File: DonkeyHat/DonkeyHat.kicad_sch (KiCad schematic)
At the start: 11 parts, among them J1 GPIO, J2 Conn_01x02_Pin, U1 ProMicro

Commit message: Added 4-bit encoders
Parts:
- removed Encoder: Conn_01x03_Pin, Connector_PinHeader_2.54mm:PinHeader_1x03_P2.54mm_Vertical, symbol Connector:Conn_01x03_Pin
- added J2: Encoder 2, Connector_PinHeader_2.54mm:PinHeader_1x04_P2.54mm_Vertical, symbol Connector:Conn_01x04_Pin
- added J3: Encoder 1, Connector_PinHeader_2.54mm:PinHeader_1x04_P2.54mm_Vertical, symbol Connector:Conn_01x04_Pin
- renumbered J2 to 5V1
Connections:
- net +3V3: now also J2.2 (Pin_2), J3.2 (Pin_2)
- net +5V: now also U1.22 (RST), U1.24 (RAW)
- net +BATT: no longer U1.24 (RAW)
- net GND: now also J2.1 (Pin_1), J3.1 (Pin_1)
- net GPIO13/PWM1: now also J2.3 (Pin_3)
- net GPIO16: now also J3.3 (Pin_3)
- net GPIO5: now also J3.4 (Pin_4)
- net GPIO6: now also J2.4 (Pin_4)

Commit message: Switched encoders to RP2040
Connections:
- net GPIO13/PWM1: no longer J2.3 (Pin_3)
- net GPIO16: no longer J3.3 (Pin_3)
- net GPIO5: no longer J3.4 (Pin_4)
- net GPIO6: no longer J1.31 (Pin_31), J2.4 (Pin_4)
- net at U1.10 (E6): now also J2.4 (Pin_4)
- net at U1.14 (B2): now also J3.3 (Pin_3)
- net at U1.15 (B3): now also J3.4 (Pin_4)
- net at U1.9 (D7): now also J2.3 (Pin_3)
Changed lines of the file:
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@@
-	)
-	(junction
-		(at 34.29 68.58)
-		(diameter 0)
-		(color 0 0 0 0)
 	)
 	(junction
@@
 	(wire
 		(pts
-			(xy 43.18 92.71) (xy 43.18 97.79)
-		)
-		(stroke
-			(width 0)
-			(type solid)
-		)
-	)
-	(wire
-		(pts
 			(xy 76.2 33.02) (xy 76.2 43.18)
 		)
@@
 	(wire
 		(pts
-			(xy 27.94 97.79) (xy 43.18 97.79)
-		)
-		(stroke
-			(width 0)
-			(type solid)
+			(xy 113.03 90.17) (xy 113.03 111.76)
+		)
+		(stroke
+			(width 0)
+			(type default)
 		)
 	)
@@
 	(wire
 		(pts
+			(xy 25.4 90.17) (xy 27.94 90.17)
+		)
+		(stroke
+			(width 0)
+			(type default)
+		)
+	)
+	(wire
+		(pts
 			(xy 80.01 71.12) (xy 100.33 71.12)
 		)
@@
 	(wire
 		(pts
-			(xy 15.24 66.04) (xy 60.96 66.04)
-		)
-		(stroke
-			(width 0)
-			(type solid)
-		)
-	)
-	(wire
-		(pts
 			(xy 154.94 46.99) (xy 162.56 46.99)
 		)
@@
 	(wire
 		(pts
-			(xy 25.4 90.17) (xy 34.29 90.17)
-		)
-		(stroke
-			(width 0)
-			(type solid)
-		)
-	)
-	(wire
-		(pts
 			(xy 161.29 69.85) (xy 162.56 69.85)
 		)
@@
 	(wire
 		(pts
-			(xy 25.4 92.71) (xy 25.4 97.79)
-		)
-		(stroke
-			(width 0)
-			(type solid)
-		)
-	)
-	(wire
-		(pts
 			(xy 76.2 50.8) (xy 76.2 63.5)
 		)
@@
 	(wire
 		(pts
+			(xy 115.57 109.22) (xy 115.57 92.71)
+		)
+		(stroke
+			(width 0)
+			(type default)
+		)
+	)
+	(wire
+		(pts
 			(xy 152.4 49.53) (xy 162.56 49.53)
 		)
@@
 	(wire
 		(pts
-			(xy 27.94 63.5) (xy 27.94 97.79)
-		)
-		(stroke
-			(width 0)
-			(type solid)
+			(xy 43.18 92.71) (xy 49.53 92.71)
+		)
+		(stroke
+			(width 0)
+			(type default)
 		)
 	)
@@
 	(wire
 		(pts
-			(xy 43.18 90.17) (xy 80.01 90.17)
-		)
-		(stroke
-			(width 0)
-			(type default)
-		)
-	)
-	(wire
-		(pts
 			(xy 133.35 52.07) (xy 137.16 52.07)
 		)
@@
 	(wire
 		(pts
-			(xy 15.24 66.04) (xy 15.24 97.79)
-		)
-		(stroke
-			(width 0)
-			(type solid)
+			(xy 49.53 121.92) (xy 163.83 121.92)
+		)
+		(stroke
+			(width 0)
+			(type default)
 		)
 	)
@@
 	(wire
 		(pts
-			(xy 15.24 97.79) (xy 25.4 97.79)
-		)
-		(stroke
-			(width 0)
-			(type solid)
-		)
-	)
-	(wire
-		(pts
 			(xy 152.4 36.83) (xy 162.56 36.83)
 		)
@@
 	(wire
 		(pts
+			(xy 163.83 92.71) (xy 157.48 92.71)
+		)
+		(stroke
+			(width 0)
+			(type default)
+		)
+	)
+	(wire
+		(pts
 			(xy 31.75 55.88) (xy 60.96 55.88)
 		)
@@
 	(wire
 		(pts
+			(xy 121.92 90.17) (xy 113.03 90.17)
+		)
+		(stroke
+			(width 0)
+			(type default)
+		)
+	)
+	(wire
+		(pts
 			(xy 55.88 48.26) (xy 60.96 48.26)
 		)
@@
 	(wire
 		(pts
+			(xy 162.56 95.25) (xy 162.56 116.84)
+		)
+		(stroke
+			(width 0)
+			(type default)
+		)
+	)
+	(wire
+		(pts
 			(xy 124.46 41.91) (xy 134.62 41.91)
 		)
@@
 	(wire
 		(pts
+			(xy 46.99 90.17) (xy 43.18 90.17)
+		)
+		(stroke
+			(width 0)
+			(type default)
+		)
+	)
+	(wire
+		(pts
 			(xy 157.48 74.93) (xy 161.29 74.93)
 		)
@@
 	(wire
 		(pts
+			(xy 113.03 111.76) (xy 27.94 111.76)
+		)
+		(stroke
+			(width 0)
+			(type default)
+		)
+	)
+	(wire
+		(pts
 			(xy 73.66 40.64) (xy 100.33 40.64)
 		)
@@
 	(wire
 		(pts
+			(xy 49.53 92.71) (xy 49.53 121.92)
+		)
+		(stroke
+			(width 0)
+			(type default)
+		)
+	)
+	(wire
+		(pts
 			(xy 69.85 93.98) (xy 72.39 93.98)
 		)
@@
 	(wire
 		(pts
+			(xy 25.4 92.71) (xy 25.4 109.22)
+		)
+		(stroke
+			(width 0)
+			(type default)
+		)
+	)
+	(wire
+		(pts
 			(xy 166.37 106.68) (xy 166.37 72.39)
 		)
@@
 	(wire
 		(pts
+			(xy 115.57 92.71) (xy 121.92 92.71)
+		)
+		(stroke
+			(width 0)
+			(type default)
+		)
+	)
+	(wire
+		(pts
 			(xy 132.08 26.67) (xy 119.38 26.67)
 		)
@@
 	(wire
 		(pts
+			(xy 46.99 116.84) (xy 46.99 90.17)
+		)
+		(stroke
+			(width 0)
+			(type default)
+		)
+	)
+	(wire
+		(pts
 			(xy 41.91 15.24) (xy 49.53 15.24)
 		)
@@
 	(wire
 		(pts
+			(xy 157.48 95.25) (xy 162.56 95.25)
+		)
+		(stroke
+			(width 0)
+			(type default)
+		)
+	)
+	(wire
+		(pts
 			(xy 50.8 87.63) (xy 72.39 87.63)
 		)
@@
 	(wire
 		(pts
-			(xy 34.29 68.58) (xy 34.29 90.17)
-		)
-		(stroke
-			(width 0)
-			(type solid)
-		)
-	)
-	(wire
-		(pts
 			(xy 26.67 30.48) (xy 60.96 30.48)
 		)
@@
 	(wire
 		(pts
+			(xy 163.83 121.92) (xy 163.83 92.71)
+		)
+		(stroke
+			(width 0)
+			(type default)
+		)
+	)
+	(wire
+		(pts
 			(xy 137.16 34.29) (xy 132.08 34.29)
 		)
@@
 	(wire
 		(pts
+			(xy 162.56 116.84) (xy 46.99 116.84)
+		)
+		(stroke
+			(width 0)
+			(type default)
+		)
+	)
+	(wire
+		(pts
 			(xy 73.66 53.34) (xy 100.33 53.34)
 		)
@@
 	(wire
 		(pts
-			(xy 60.96 68.58) (xy 34.29 68.58)
-		)
-		(stroke
-			(width 0)
-			(type solid)
-		)
-	)
-	(wire
-		(pts
 			(xy 147.32 57.15) (xy 152.4 57.15)
 		)
@@
 	(wire
 		(pts
-			(xy 34.29 68.58) (xy 31.75 68.58)
+			(xy 25.4 109.22) (xy 115.57 109.22)
+		)
+		(stroke
+			(width 0)
+			(type default)
+		)
+	)
+	(wire
+		(pts
+			(xy 31.75 68.58) (xy 60.96 68.58)
 		)
 		(stroke
@@
 		)
 		(stroke
+			(width 0)
+			(type default)
+		)
+	)
+	(wire
+		(pts
+			(xy 27.94 111.76) (xy 27.94 90.17)
+		)
+		(stroke

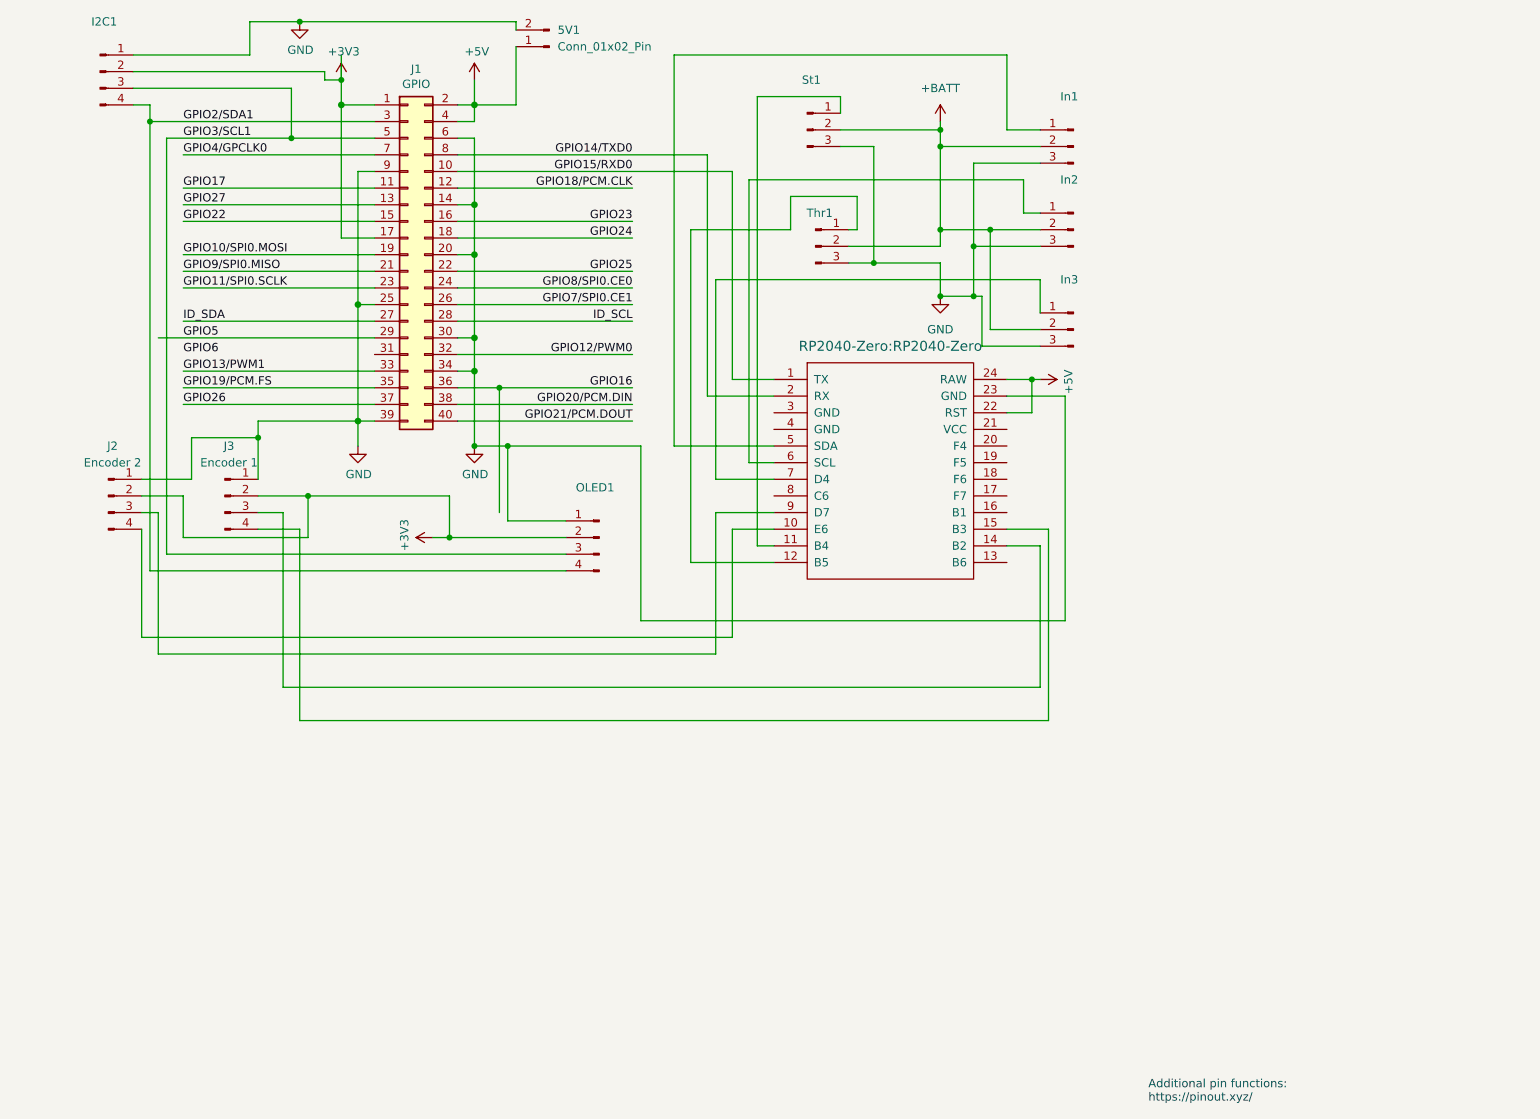
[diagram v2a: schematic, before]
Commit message: catellated pins
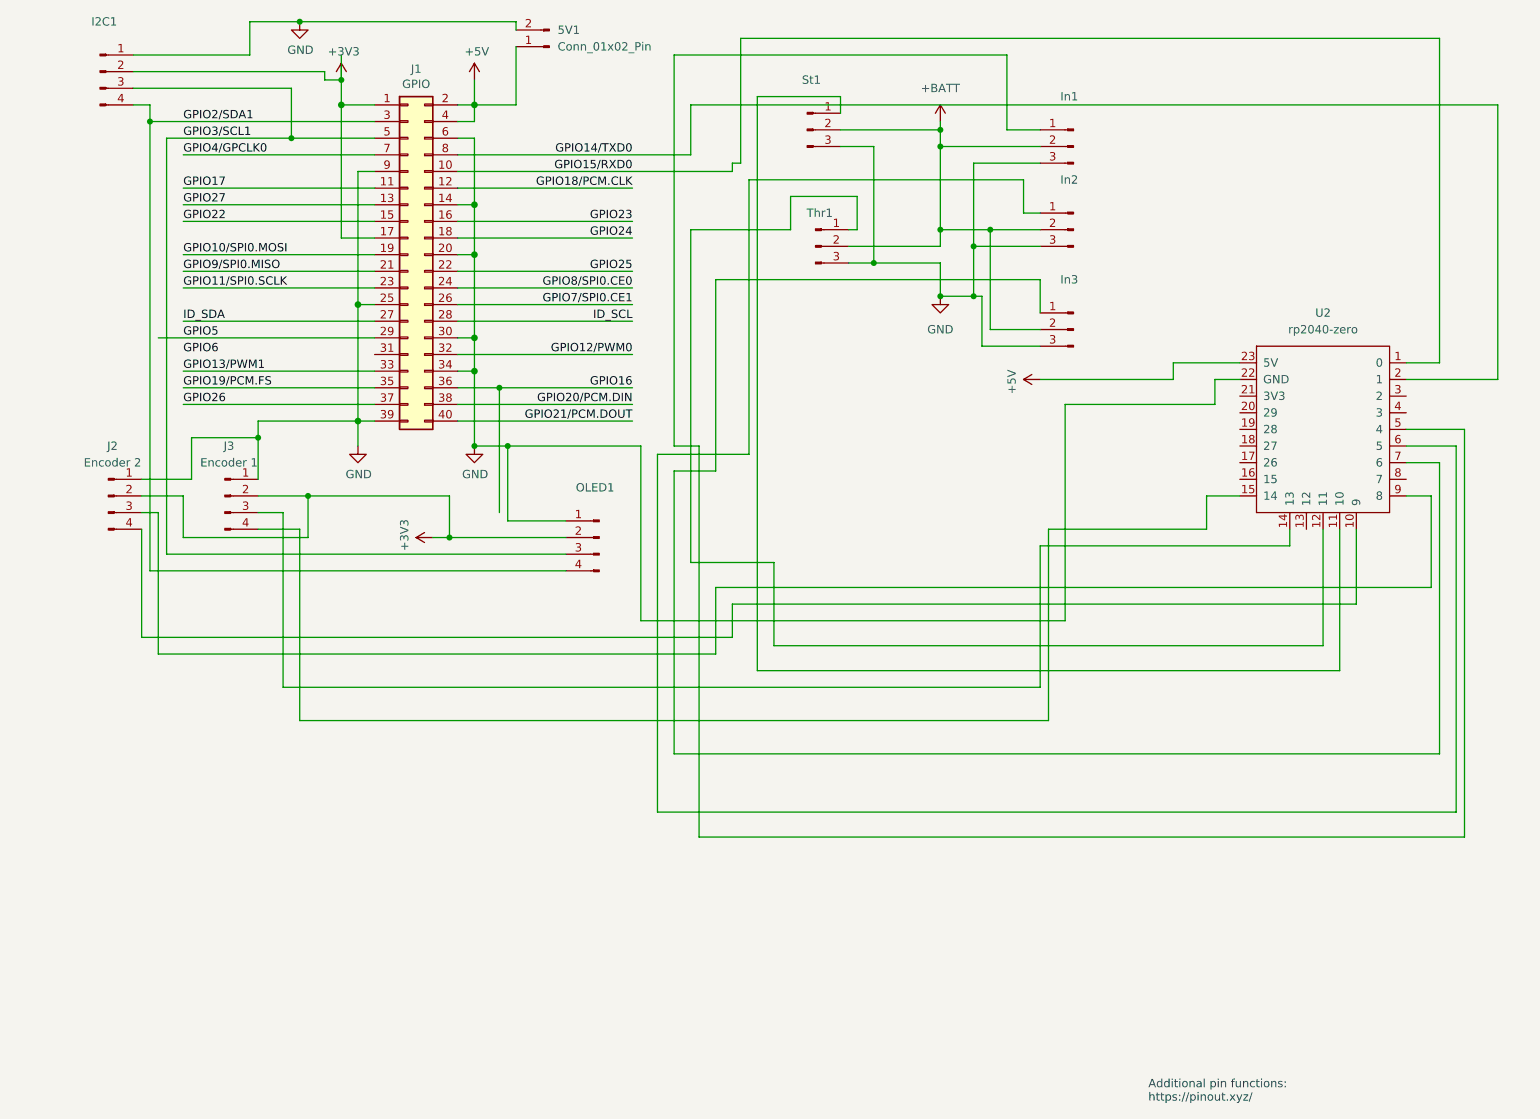
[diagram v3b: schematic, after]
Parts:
- removed U1: ProMicro, RP2040-Zero:RP2040-Zero, symbol promicro:ProMicro
- added U2: rp2040-zero, symbol mcu:rp2040-zero
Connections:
- net +5V: now also U2.23 (5V)
- net GND: now also U2.22 (GND)
- net GPIO14/TXD0: now also U2.2 (1)
- net GPIO15/RXD0: now also U2.1 (0)
- net at Thr1.1 (Pin_1): now also U2.12 (11)
- net at J2.3 (Pin_3): now also U2.9 (8)
- net at J2.4 (Pin_4): now also U2.10 (9)
- net at St1.1 (Pin_1): now also U2.11 (10)
- net at J3.3 (Pin_3): now also U2.14 (13)
- net at J3.4 (Pin_4): now also U2.15 (14)
- net at In1.1 (Pin_1): now also U2.5 (4)
- net at In2.1 (Pin_1): now also U2.6 (5)
- net at In3.1 (Pin_1): now also U2.7 (6)

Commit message: routed
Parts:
- U2: footprint (none) -> mcu:rp2040-zero-tht
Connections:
- net at J2.3 (Pin_3): now also U2.16 (15); no longer U2.9 (8)
- net at J3.3 (Pin_3): now also U2.19 (28); no longer U2.14 (13)
- net at U2.17 (26): now also In2.1 (Pin_1)
- net at U2.18 (27): now also In3.1 (Pin_1)
- net at U2.20 (29): now also In1.1 (Pin_1)
- net at U2.5 (4): no longer In1.1 (Pin_1)
- net at U2.6 (5): no longer In2.1 (Pin_1)
- net at U2.7 (6): no longer In3.1 (Pin_1)
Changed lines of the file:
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@@
-	(wire
-		(pts
-			(xy 226.06 135.89) (xy 226.06 80.01)
-		)
-		(stroke
-			(width 0)
-			(type default)
-		)
-	)
 	(wire
 		(pts
@@
 	(wire
 		(pts
+			(xy 193.04 80.01) (xy 186.69 80.01)
+		)
+		(stroke
+			(width 0)
+			(type default)
+		)
+	)
+	(wire
+		(pts
 			(xy 162.56 54.61) (xy 162.56 59.69)
 		)
@@
 	(wire
 		(pts
-			(xy 222.25 101.6) (xy 222.25 87.63)
-		)
-		(stroke
-			(width 0)
-			(type default)
-		)
-	)
-	(wire
-		(pts
 			(xy 208.28 92.71) (xy 208.28 114.3)
 		)
@@
 	(wire
 		(pts
+			(xy 162.56 77.47) (xy 193.04 77.47)
+		)
+		(stroke
+			(width 0)
+			(type default)
+		)
+	)
+	(wire
+		(pts
 			(xy 58.42 38.1) (xy 60.96 38.1)
 		)
@@
 	(wire
 		(pts
+			(xy 193.04 85.09) (xy 190.5 85.09)
+		)
+		(stroke
+			(width 0)
+			(type default)
+		)
+	)
+	(wire
+		(pts
 			(xy 182.88 69.85) (xy 182.88 67.31)
 		)
@@
 	(wire
 		(pts
-			(xy 104.14 135.89) (xy 226.06 135.89)
+			(xy 185.42 82.55) (xy 193.04 82.55)
+		)
+		(stroke
+			(width 0)
+			(type default)
+		)
+	)
+	(wire
+		(pts
+			(xy 104.14 135.89) (xy 185.42 135.89)
 		)
 		(stroke
@@
 	(wire
 		(pts
+			(xy 162.56 77.47) (xy 162.56 116.84)
+		)
+		(stroke
+			(width 0)
+			(type default)
+		)
+	)
+	(wire
+		(pts
 			(xy 80.01 90.17) (xy 80.01 71.12)
 		)
@@
 	(wire
 		(pts
-			(xy 223.52 127) (xy 223.52 82.55)
+			(xy 190.5 85.09) (xy 190.5 101.6)
 		)
 		(stroke
@@
 	(wire
 		(pts
-			(xy 162.56 95.25) (xy 162.56 116.84)
-		)
-		(stroke
-			(width 0)
-			(type default)
-		)
-	)
-	(wire
-		(pts
 			(xy 124.46 41.91) (xy 134.62 41.91)
 		)
@@
 	(wire
 		(pts
-			(xy 227.33 139.7) (xy 227.33 77.47)
-		)
-		(stroke
-			(width 0)
-			(type default)
-		)
-	)
-	(wire
-		(pts
 			(xy 55.88 27.94) (xy 55.88 48.26)
 		)
@@
 	(wire
 		(pts
-			(xy 218.44 87.63) (xy 222.25 87.63)
-		)
-		(stroke
-			(width 0)
-			(type default)
-		)
-	)
-	(wire
-		(pts
-			(xy 106.68 127) (xy 223.52 127)
+			(xy 106.68 127) (xy 186.69 127)
 		)
 		(stroke
@@
 	(wire
 		(pts
+			(xy 185.42 82.55) (xy 185.42 135.89)
+		)
+		(stroke
+			(width 0)
+			(type default)
+		)
+	)
+	(wire
+		(pts
 			(xy 73.66 48.26) (xy 100.33 48.26)
 		)
@@
 	(wire
 		(pts
-			(xy 162.56 95.25) (xy 200.66 95.25)
-		)
-		(stroke
-			(width 0)
-			(type default)
-		)
-	)
-	(wire
-		(pts
-			(xy 113.03 101.6) (xy 222.25 101.6)
+			(xy 181.61 74.93) (xy 181.61 139.7)
+		)
+		(stroke
+			(width 0)
+			(type default)
+		)
+	)
+	(wire
+		(pts
+			(xy 113.03 101.6) (xy 190.5 101.6)
 		)
 		(stroke
@@
 	(wire
 		(pts
+			(xy 186.69 80.01) (xy 186.69 127)
+		)
+		(stroke
+			(width 0)
+			(type default)
+		)
+	)
+	(wire
+		(pts
 			(xy 132.08 29.21) (xy 132.08 26.67)
 		)
@@
 	(wire
 		(pts
-			(xy 227.33 77.47) (xy 218.44 77.47)
-		)
-		(stroke
-			(width 0)
-			(type default)
-		)
-	)
-	(wire
-		(pts
 			(xy 76.2 33.02) (xy 73.66 33.02)
 		)
@@
 	(wire
 		(pts
-			(xy 200.66 92.71) (xy 200.66 95.25)
-		)
-		(stroke
-			(width 0)
-			(type default)
-		)
-	)
-	(wire
-		(pts
 			(xy 187.96 92.71) (xy 187.96 87.63)
 		)
@@
 	(wire
 		(pts
-			(xy 223.52 82.55) (xy 218.44 82.55)
-		)
-		(stroke
-			(width 0)
-			(type default)
-		)
-	)
-	(wire
-		(pts
 			(xy 43.18 78.74) (xy 43.18 85.09)
 		)
@@
 	(wire
 		(pts
+			(xy 193.04 74.93) (xy 181.61 74.93)
+		)
+		(stroke
+			(width 0)
+			(type default)
+		)
+	)
+	(wire
+		(pts
 			(xy 106.68 20.32) (xy 157.48 20.32)
 		)
@@
 	(wire
 		(pts
-			(xy 226.06 80.01) (xy 218.44 80.01)
-		)
-		(stroke
-			(width 0)
-			(type default)
-		)
-	)
-	(wire
-		(pts
-			(xy 110.49 139.7) (xy 227.33 139.7)
+			(xy 110.49 139.7) (xy 181.61 139.7)
 		)
 		(stroke
@@
 			)
 		)
-		(property "Footprint" ""
+		(property "Footprint" "mcu:rp2040-zero-tht"
 			(at 196.85 71.12 0)
 			(effects

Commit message: Typo
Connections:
- net at U2.16 (15): no longer J2.3 (Pin_3)
- net at U2.10 (9): no longer J2.4 (Pin_4)
- net at U2.19 (28): no longer J3.3 (Pin_3)
- net at U2.15 (14): no longer J3.4 (Pin_4)
- net Enc2A: now reaches U2.13 (12)
- net Enc2A: now also J2.3 (Pin_3)
- net Enc2B: now reaches U2.14 (13)
- net Enc2B: now also J2.4 (Pin_4)
- net Enc1A: now reaches U2.8 (7)
- net Enc1A: now also J3.3 (Pin_3)
- net Enc1B: now reaches U2.9 (8)
- net Enc1B: now also J3.4 (Pin_4)

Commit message: New PCB
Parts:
- added J4: B4B-PH-K-S_LF__SN_, Connector_JST:JST_SH_BM04B-SRSS-TB_1x04-1MP_P1.00mm_Vertical, symbol dk_Rectangular-Connectors-Headers-Male-Pins:B4B-PH-K-S_LF__SN_
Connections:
- net +3V3: now also J4.3
- net GND: now also J4.4
- net GPIO2/SDA1: now also J4.2
- net GPIO3/SCL1: now also J4.1

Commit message: WIP
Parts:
- removed In1: RC 1, Connector_PinHeader_2.54mm:PinHeader_1x03_P2.54mm_Vertical, symbol Connector:Conn_01x03_Pin
- removed In2, St1, Thr1: Conn_01x03_Pin, Connector_PinHeader_2.54mm:PinHeader_1x03_P2.54mm_Vertical, symbol Connector:Conn_01x03_Pin
- added H1, H2, H3: MountingHole, symbol Mechanical:MountingHole
- added J5, J6: Conn_02x03_Odd_Even, Connector_PinHeader_2.54mm:PinHeader_2x03_P2.54mm_Vertical, symbol Connector_Generic:Conn_02x03_Odd_Even
- J4: value B4B-PH-K-S_LF__SN_ -> I2C
- renumbered In3 to Throttle1
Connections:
- net +BATT is gone; now on net +5V: Throttle1.2 (Pin_2)
- net +5V: now also J5.3 (Pin_3), J5.4 (Pin_4), J6.3 (Pin_3), J6.4 (Pin_4)
- net GND: now also Throttle1.1 (Pin_1), J5.1 (Pin_1), J5.2 (Pin_2), J6.1 (Pin_1), J6.2 (Pin_2); no longer Throttle1.3 (Pin_3)
- net GPIO14/TXD0: no longer U2.2 (1)
- net GPIO15/RXD0: no longer J1.10 (Pin_10), U2.1 (0)
- net Steer: now reaches U2.12 (11)
- net Steer: now also J5.6 (Pin_6)
- net Throttle: now reaches U2.11 (10)
- net Throttle: now also J5.5 (Pin_5)
- net RCin2: now reaches U2.17 (26)
- net RCin2: now also J6.5 (Pin_5)
- net RCin1: now reaches U2.18 (27)
- net RCin1: now also J6.6 (Pin_6); no longer Throttle1.1 (Pin_1)
- net RCin3: now reaches U2.20 (29)
- net RCin3: now also Throttle1.3 (Pin_3)
